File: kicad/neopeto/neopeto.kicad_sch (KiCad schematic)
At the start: 144 parts, among them J1 Conn_01x10_Pin, J2 Conn_01x10_Pin, J3 Conn_01x10_Pin, J4 PJ-307, U1 74HC00, U10 74HC590, U11 74HC590, U12 74HC590, U13 74HC245, U14 K6X4008C1F, U15 74HC245, U16 74HC245, U17 LM358LV, U18 LM358LV, U19 LM358LV, U2 74LVC1G00, U21 TLC7258C, U22 TLC7258C, U23 74HC4017, U24 74HC86, U25 74AUP1G08, U26 74LVC1G332, U27 74LVC1G332, U3 CH32V003JxMx, U4 82C55A_PLCC, U5 82C54_PLCC, U6 74HC139, U7 74HC245, U8 74HC245, U9 74HC245, X1 ECS-2520MV-12MHZ

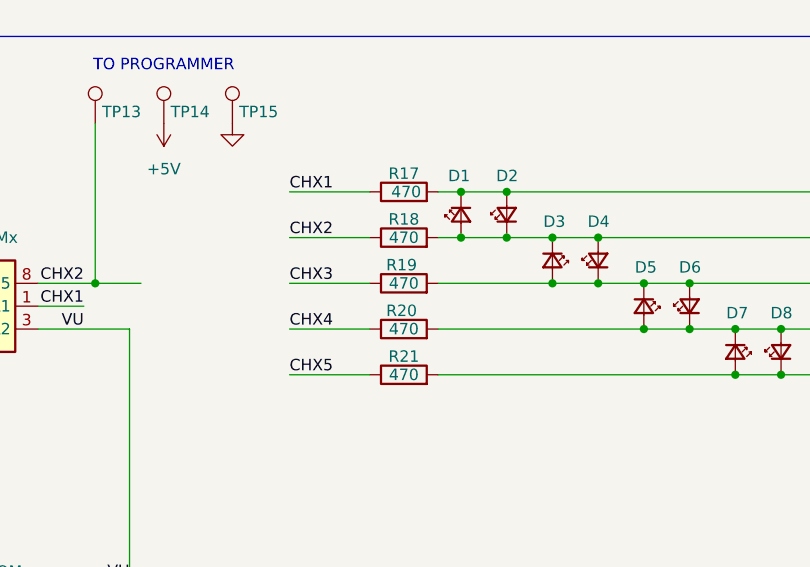
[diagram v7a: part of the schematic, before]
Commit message: update led resistor values
470*2 / 20 makes for a rather dim display
the leds are specified for 25mA at 1.6V

100 ohm * 2 -> 17mA, bright enough not to look good next to other leds
on my desk and on the same board
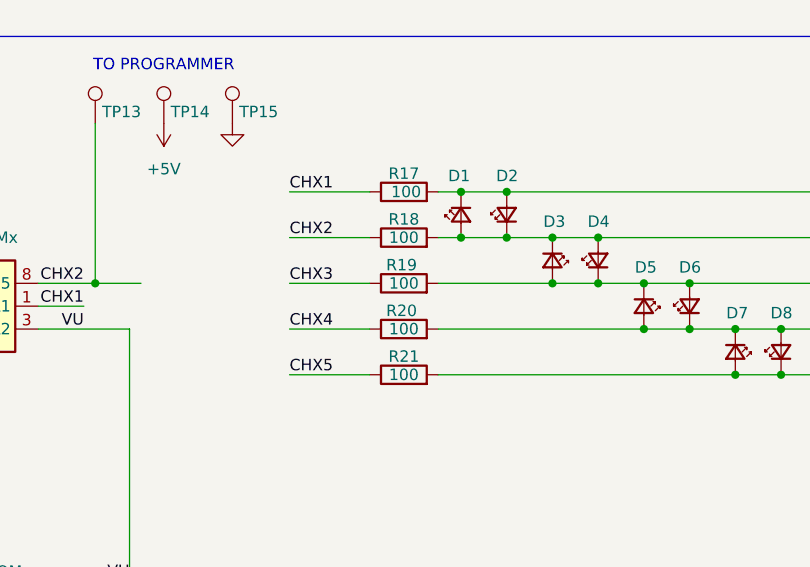
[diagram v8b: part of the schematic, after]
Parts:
- R17, R18, R19, R20, R21: value 470 -> 100
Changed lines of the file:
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@@
 			)
 		)
-		(property "Value" "470"
+		(property "Value" "100"
 			(at 463.55 259.08 90)
 			(effects
@@
 			)
 		)
-		(property "Value" "470"
+		(property "Value" "100"
 			(at 463.55 248.92 90)
 			(effects
@@
 			)
 		)
-		(property "Value" "470"
+		(property "Value" "100"
 			(at 463.804 238.76 90)
 			(effects
@@
 			)
 		)
-		(property "Value" "470"
+		(property "Value" "100"
 			(at 463.55 243.84 90)
 			(effects
@@
 			)
 		)
-		(property "Value" "470"
+		(property "Value" "100"
 			(at 463.55 254 90)
 			(effects
